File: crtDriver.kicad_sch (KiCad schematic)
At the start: 66 parts, among them J1 Lum_In, J2 H_Sync, J3 V_Sync, Q1 2N7000, Q10 2N7000, Q11 2N7000, Q12 2N7000, Q13 2N7000, Q14 2N7000, Q15 2N7000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

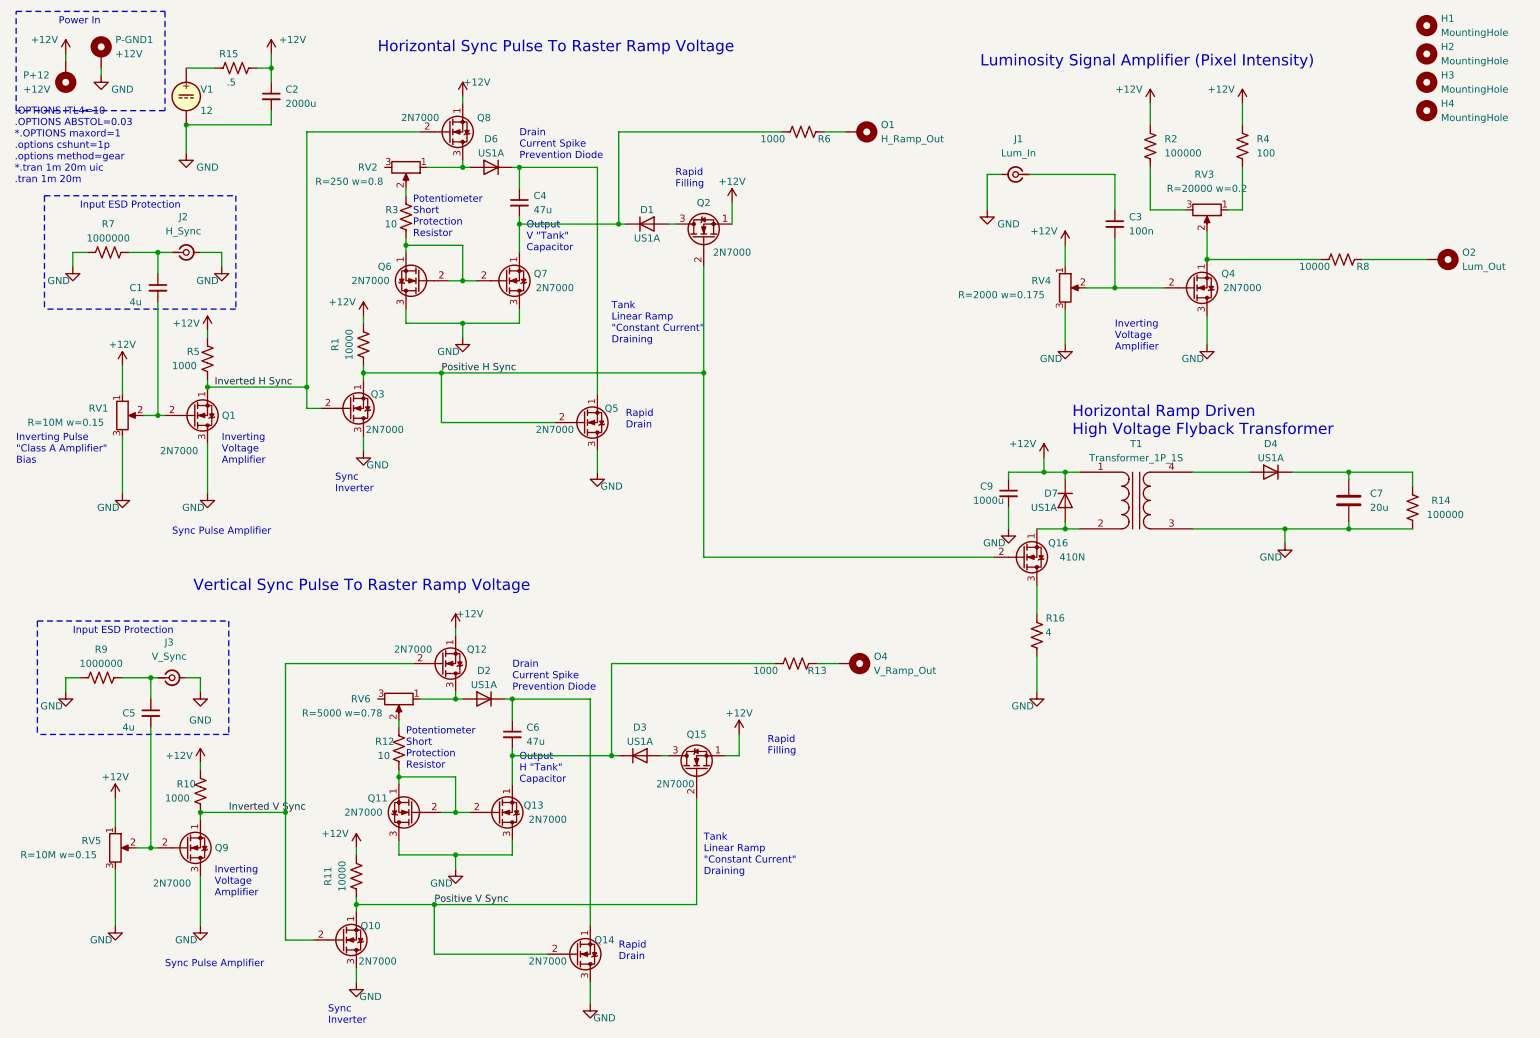
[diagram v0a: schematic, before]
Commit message: changed to hierarchical schematic sheets for electron microscope components (pump motor controllers, focusing coils, etc)
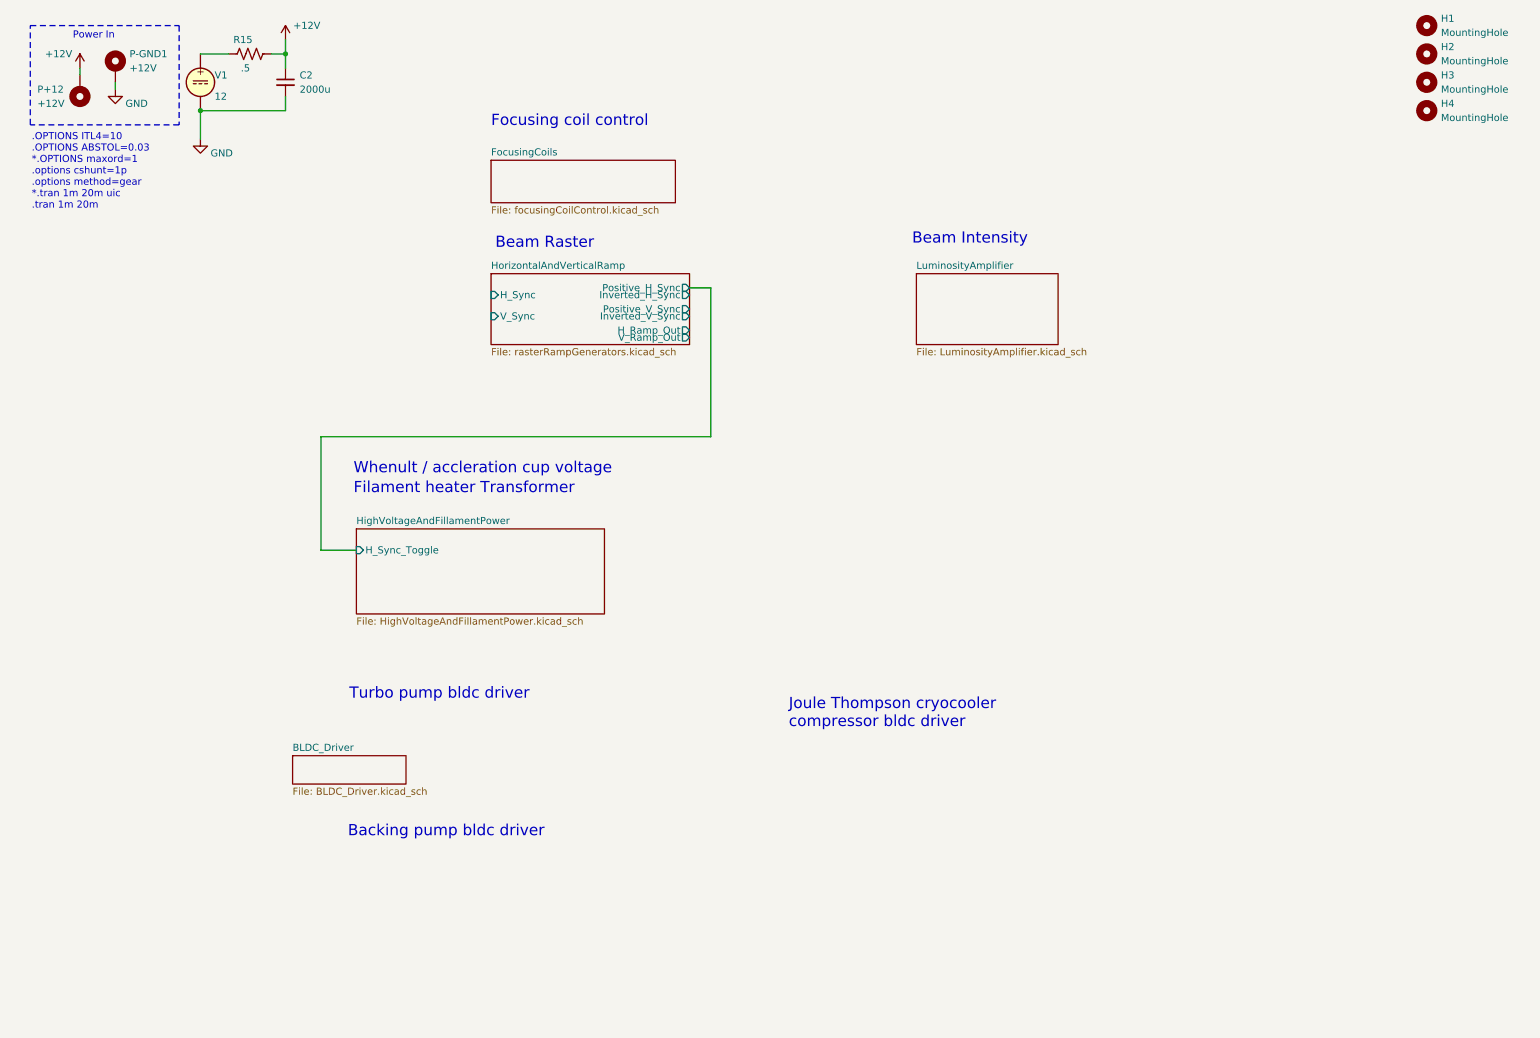
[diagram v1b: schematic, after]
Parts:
- removed C1, C5: 4u, Capacitor_SMD:C_0603_1608Metric, symbol Device:C_Small
- removed C3: 100n, Capacitor_SMD:C_0603_1608Metric, symbol Device:C_Small
- removed C4, C6: 47u, Capacitor_SMD:C_1206_3216Metric, symbol Device:C_Small
- removed C7: 20u, Capacitor_SMD:C_0603_1608Metric, symbol Device:C
- removed C9: 1000u, Capacitor_SMD:C_1206_3216Metric, symbol Device:C_Small
- removed D1, D2, D3, D4, D6, D7: US1A, Diode_SMD:D_SMA, symbol Diode:US1A
- removed J1: Lum_In, Connector_Coaxial:SMA_Amphenol_901-144_Vertical, symbol Connector:Conn_Coaxial_Small
- removed J2: H_Sync, Connector_Coaxial:SMA_Amphenol_901-144_Vertical, symbol Connector:Conn_Coaxial_Small
- removed J3: V_Sync, Connector_Coaxial:SMA_Amphenol_901-144_Vertical, symbol Connector:Conn_Coaxial_Small
- removed O1: H_Ramp_Out, Connector_Wire:SolderWire-0.25sqmm_1x01_D0.65mm_OD2mm_Relief, symbol Mechanical:MountingHole_Pad
- removed O2: Lum_Out, Connector_Wire:SolderWire-0.25sqmm_1x01_D0.65mm_OD2mm_Relief, symbol Mechanical:MountingHole_Pad
- removed O4: V_Ramp_Out, Connector_Wire:SolderWire-0.25sqmm_1x01_D0.65mm_OD2mm_Relief, symbol Mechanical:MountingHole_Pad
- removed Q1, Q10, Q11, Q12, Q13, Q14, Q15, Q2, Q3, Q4, Q5, Q6, Q7, Q8, Q9: 2N7000, Package_TO_SOT_SMD:SOT-23, symbol Transistor_FET:2N7000
- removed Q16: 410N, Package_TO_SOT_SMD:SOT-23, symbol Transistor_FET:2N7000
- removed R1, R11, R8: 10000, Resistor_SMD:R_0603_1608Metric, symbol Device:R_US
- removed R10, R5: 1000, Resistor_SMD:R_1210_3225Metric, symbol Device:R_US
- removed R12, R3: 10, Resistor_SMD:R_1210_3225Metric, symbol Device:R_US
- removed R13, R6: 1000, Resistor_SMD:R_0603_1608Metric, symbol Device:R_US
- removed R14: 100000, Resistor_SMD:R_0603_1608Metric, symbol Device:R_US
- removed R16: 4, Resistor_SMD:R_0603_1608Metric, symbol Device:R_US
- removed R2: 100000, Resistor_SMD:R_0805_2012Metric, symbol Device:R_US
- removed R4: 100, Resistor_SMD:R_0805_2012Metric, symbol Device:R_US
- removed R7, R9: 1000000, Resistor_SMD:R_0603_1608Metric, symbol Device:R_US
- removed RV1, RV4, RV5: 2M, Potentiometer_SMD:Potentiometer_Bourns_TC33X_Vertical, symbol Device:R_Potentiometer
- removed RV2: 250, Potentiometer_SMD:Potentiometer_Bourns_TC33X_Vertical, symbol Device:R_Potentiometer
- removed RV3: 2000, Potentiometer_SMD:Potentiometer_Bourns_TC33X_Vertical, symbol Device:R_Potentiometer
- removed RV6: 5000, Potentiometer_SMD:Potentiometer_Bourns_TC33X_Vertical, symbol Device:R_Potentiometer
- removed T1: Transformer_1P_1S, Transformer_SMD:Transformer_Wuerth_750315371, symbol Device:Transformer_1P_1S
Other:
- added sheet BLDC_Driver (BLDC_Driver.kicad_sch)
- added sheet FocusingCoils (focusingCoilControl.kicad_sch)
- added sheet HighVoltageAndFillamentPower (HighVoltageAndFillamentPower.kicad_sch)
- added sheet HorizontalAndVerticalRamp (rasterRampGenerators.kicad_sch)
- added sheet LuminosityAmplifier (LuminosityAmplifier.kicad_sch)
- note added: "Backing pump bldc driver"
- note added: "Beam Intensity"
- note added: "Beam Raster"
- note added: "Filament heater Transformer"
- note added: "Focusing coil control"
- note added: "Joule Thompson cryocooler compressor bldc driver"
- note added: "Turbo pump bldc driver"
- note added: "Whenult / accleration cup voltage"
- note removed: "Drain Current Spike Prevention Diode"
- note removed: "Horizontal Ramp Driven High Voltage Flyback Transformer"
- note removed: "Horizontal Sync Pulse To Raster Ramp Voltage"
- note removed: "Input ESD Protection"
- note removed: "Inverting Pulse "Class A Amplifier" Bias"
- note removed: "Inverting Voltage Amplifier"
- note removed: "Luminosity Signal Amplifier (Pixel Intensity)"
- note removed: "Output H "Tank" Capacitor"
- note removed: "Output V "Tank" Capacitor"
- note removed: "Potentiometer Short Protection Resistor"
- note removed: "Rapid Drain"
- note removed: "Rapid Filling"
- note removed: "Sync Inverter"
- note removed: "Sync Pulse Amplifier"
- note removed: "Tank Linear Ramp "Constant Current" Draining"
- note removed: "Vertical Sync Pulse To Raster Ramp Voltage"
- moved on the sheet: C2, P+12, P-GND1, R15, V1

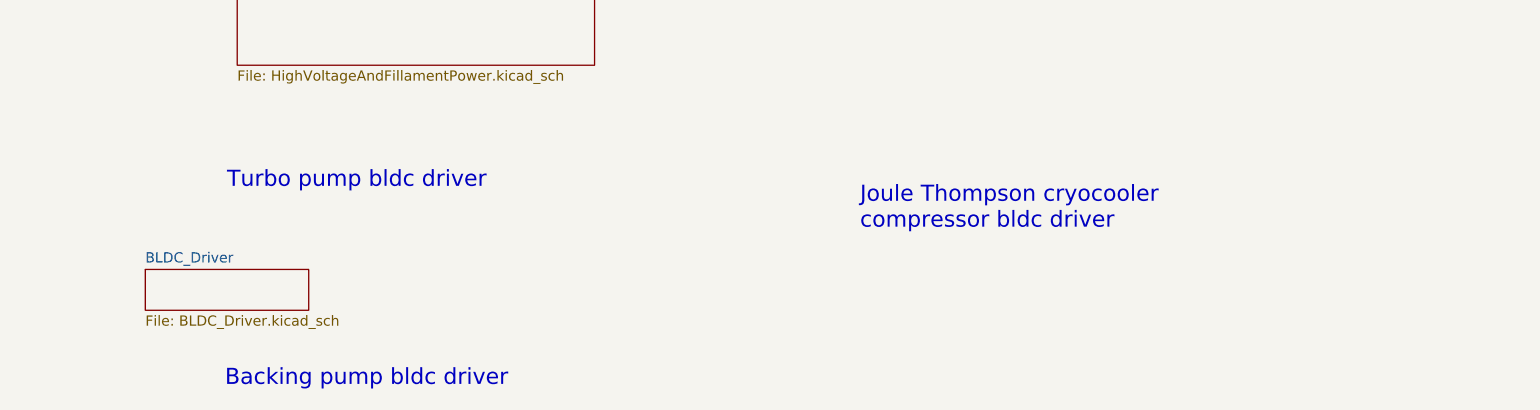
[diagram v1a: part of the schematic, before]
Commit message: added more untested ideas for schematics
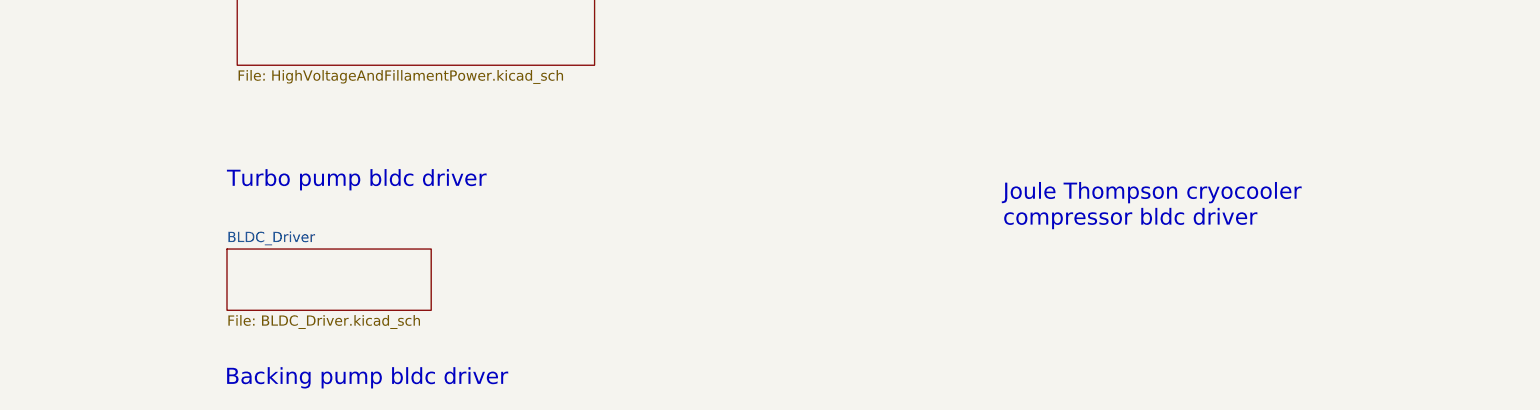
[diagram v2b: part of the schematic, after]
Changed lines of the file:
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@@
 	(text "Joule Thompson cryocooler\ncompressor bldc driver"
 		(exclude_from_sim no)
-		(at 152.4 142.494 0)
+		(at 170.18 142.24 0)
 		(effects
 			(font
@@
 	)
 	(sheet
-		(at 63.5 147.32)
-		(size 20.32 5.08)
+		(at 73.66 144.78)
+		(size 25.4 7.62)
 		(fields_autoplaced yes)
 		(stroke
@@
 		)
 		(property "Sheetname" "BLDC_Driver"
-			(at 63.5 146.6084 0)
+			(at 73.66 144.0684 0)
 			(effects
 				(font
@@
 		)
 		(property "Sheetfile" "BLDC_Driver.kicad_sch"
-			(at 63.5 152.9846 0)
-			(effects
-				(font
+			(at 73.66 152.9846 0)
+			(effects
+				(font

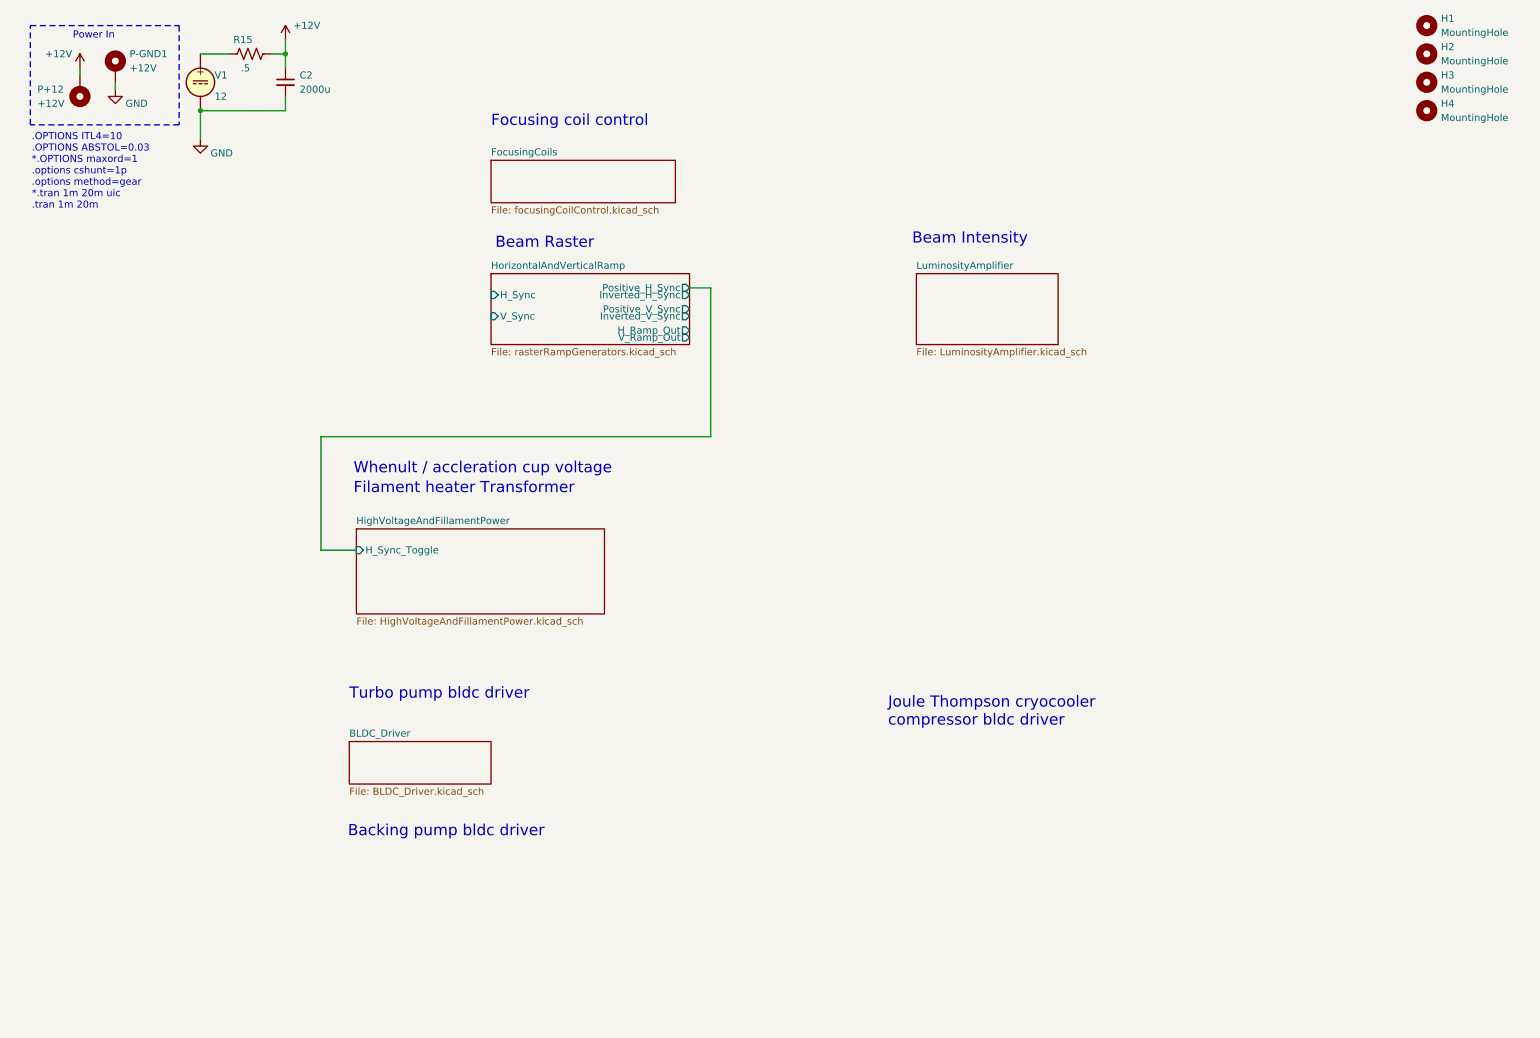
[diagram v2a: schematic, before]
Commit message: linked models so spice simulation runs
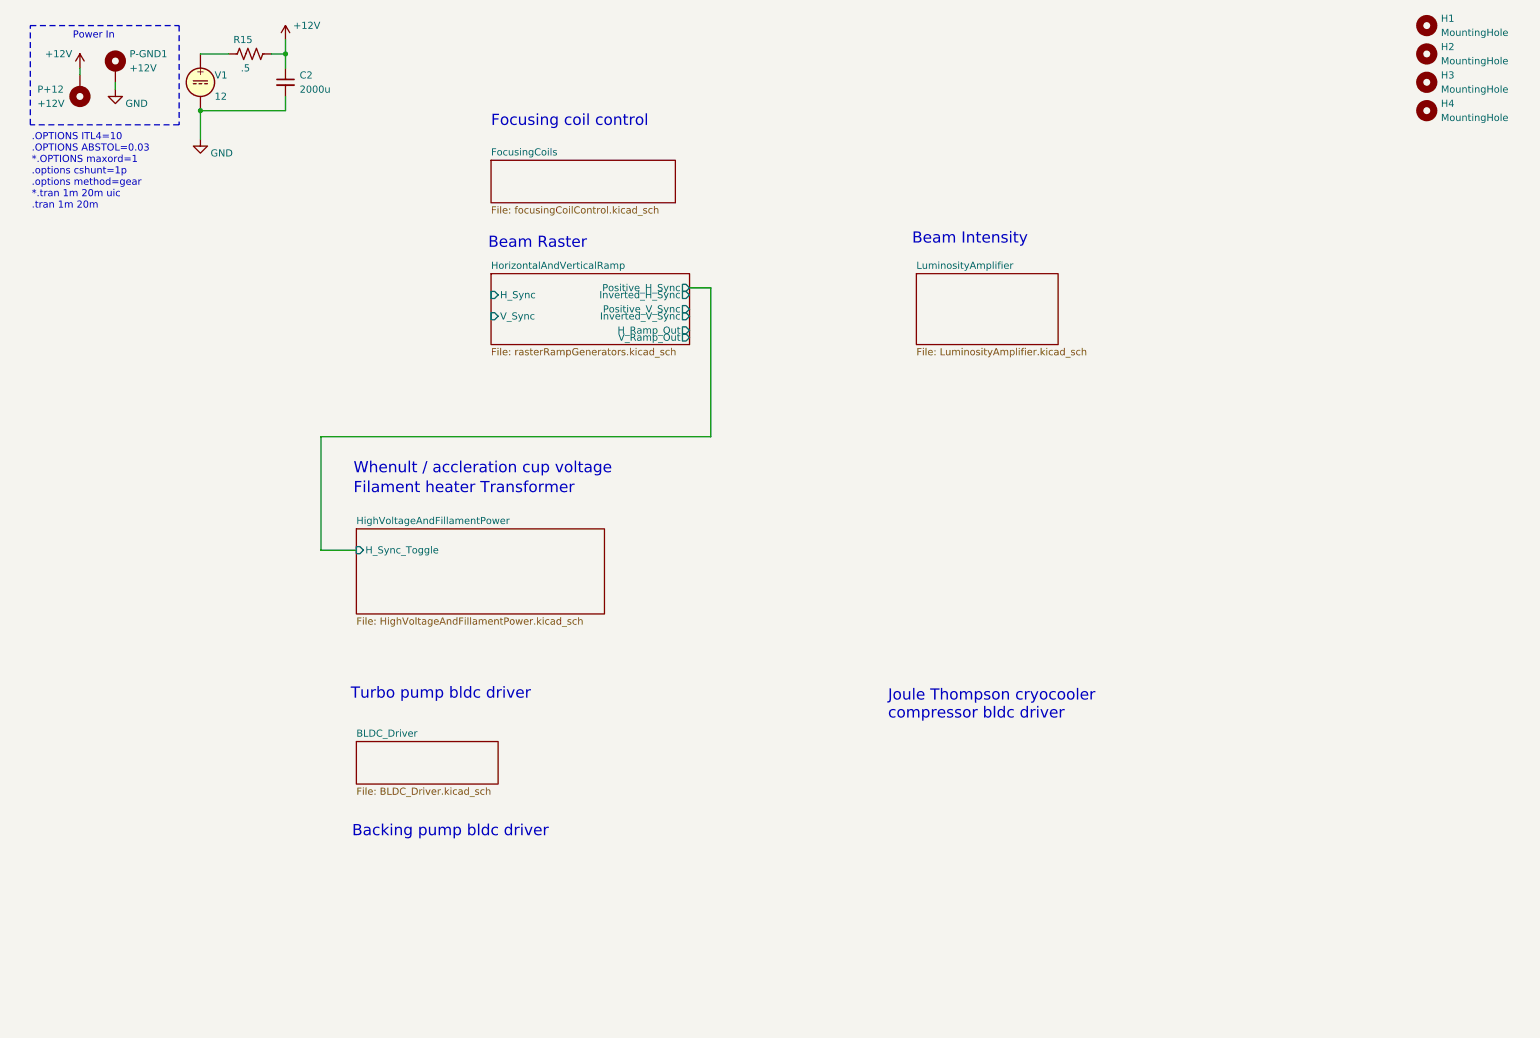
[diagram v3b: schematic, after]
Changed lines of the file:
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@@
 	(text "Joule Thompson cryocooler\ncompressor bldc driver"
 		(exclude_from_sim no)
-		(at 170.18 142.24 0)
+		(at 170.18 140.97 0)
 		(effects
 			(font
@@
 	(text "Turbo pump bldc driver"
 		(exclude_from_sim no)
-		(at 73.66 137.414 0)
+		(at 73.914 137.414 0)
 		(effects
 			(font
@@
 	(text "Backing pump bldc driver"
 		(exclude_from_sim no)
-		(at 73.406 162.052 0)
+		(at 74.168 162.052 0)
 		(effects
 			(font
@@
 	(text "Beam Raster"
 		(exclude_from_sim no)
-		(at 99.822 56.642 0)
+		(at 98.552 56.642 0)
 		(effects
 			(font
@@
 	)
 	(sheet
-		(at 73.66 144.78)
+		(at 74.93 144.78)
 		(size 25.4 7.62)
 		(fields_autoplaced yes)
@@
 		)
 		(property "Sheetname" "BLDC_Driver"
-			(at 73.66 144.0684 0)
+			(at 74.93 144.0684 0)
 			(effects
 				(font
@@
 		)
 		(property "Sheetfile" "BLDC_Driver.kicad_sch"
-			(at 73.66 152.9846 0)
-			(effects
-				(font
+			(at 74.93 152.9846 0)
+			(effects
+				(font
